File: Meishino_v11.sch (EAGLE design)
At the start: 31 parts, among them CN5 CON_AVRISPTH, CN9 CON_USB-BMICRO-B_PCB, Q1 TR_NMOS_2N7000, U1 IC_FT232RQ, U2 MCU_ATMEGA328P_ARDUINO_DIP28, U3 MOD_AE_FT232_DIP24

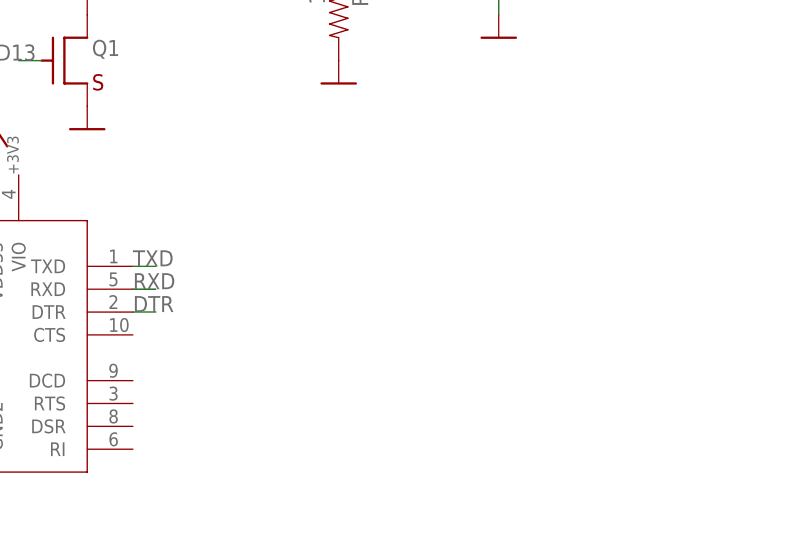
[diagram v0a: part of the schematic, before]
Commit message: リセットとネジ穴を追加、シルクの調整。
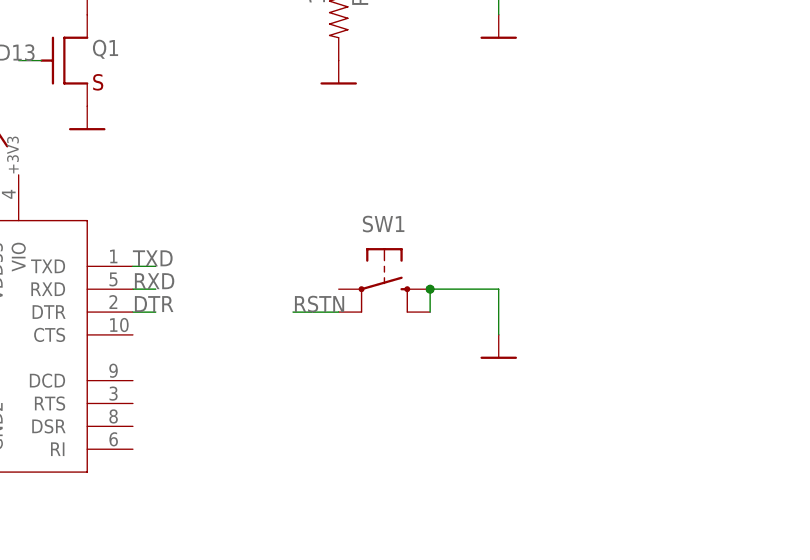
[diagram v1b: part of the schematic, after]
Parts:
- added SW1: (no value), akita:SW_TACTTH
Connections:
- net GND: now also SW1.S, SW1.S1
- net RSTN: now also SW1.P1
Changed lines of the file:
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@@
 <?xml version="1.0" encoding="utf-8"?>
 <!DOCTYPE eagle SYSTEM "eagle.dtd">
-<eagle version="9.1.0">
+<eagle version="9.0.1">
 <drawing>
 <settings>
@@
 <part name="P+11" library="akita" deviceset="POW_+5V" device=""/>
 <part name="+3V3" library="akita" deviceset="POW_+3V3" device=""/>
+<part name="SW1" library="akita" deviceset="SW_TACT" device="TH"/>
+<part name="GND14" library="akita" deviceset="POW_GND" device=""/>
 </parts>
 <sheets>
@@
 <instance part="P+11" gate="1" x="99.06" y="5.08"/>
 <instance part="+3V3" gate="G$1" x="101.6" y="5.08"/>
+<instance part="SW1" gate="1" x="144.78" y="-12.7" rot="R270"/>
+<instance part="GND14" gate="1" x="157.48" y="-20.32"/>
 </instances>
 <busses>
@@
 <pinref part="Q1" gate="G$1" pin="S"/>
 </segment>
+<segment>
+<pinref part="SW1" gate="1" pin="S1"/>
+<pinref part="SW1" gate="1" pin="S"/>
+<wire x1="149.86" y1="-15.24" x2="149.86" y2="-12.7" width="0.1524" layer="91"/>
+<wire x1="149.86" y1="-12.7" x2="157.48" y2="-12.7" width="0.1524" layer="91"/>
+<junction x="149.86" y="-12.7"/>
+<pinref part="GND14" gate="1" pin="GND"/>
+<wire x1="157.48" y1="-17.78" x2="157.48" y2="-12.7" width="0.1524" layer="91"/>
+</segment>
 </net>
 <net name="+5V" class="0">
@@
 <label x="172.72" y="83.82" size="1.778" layer="95"/>
 </segment>
-</net>
+<segment>
+<pinref part="SW1" gate="1" pin="P1"/>
+<label x="134.62" y="-15.24" size="1.778" layer="95"/>
+<wire x1="139.7" y1="-15.24" x2="134.62" y2="-15.24" width="0.1524" layer="91"/>
+</segment>
+</net>
